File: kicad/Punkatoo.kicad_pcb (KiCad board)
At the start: 2 copper layers, 79 x 63.5 mm, 58 parts, among them J1 AC, J2 I/O, J3 FTDI, J4 IO 3.3v, J5 IO GND, J6 I2C, J7 Output, K1 G3MB, K2 G3MB, K3 G3MB, K4 G3MB, K5 G3MB-Relay_SolidState, Q1 BC847, Q10 BC807, Q11 BC807, Q2 BC847, Q3 BC847, Q4 BC847, Q5 BC847, Q6 BC847, Q7 BC807, Q8 BC807, Q9 BC807, SW1 Reset, SW2 Flash, U1 ESP32-WROOM-32, U2 IR RX, U3 AMS1117-3.3

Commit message: ??
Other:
- net class Default removed

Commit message: physical switching
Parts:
- removed the C2 at (83.9, 107.1)
- removed Capacitor: Ceiling_Fan_Capacitor, punkatoo:Ceiling_Fan_Capacitor
- removed D2: IR TX, LED_THT:LED_D5.0mm
- removed the J3 at (122.8, 94.2)
- removed the J4 at (147.5, 113.1)
- removed the JP1 at (133.9, 100.1)
- removed the Q1 at (133.9, 106.4)
- removed the R2 at (129.7, 106.2)
- removed R6, R7: 10, Resistor_SMD:R_0805_2012Metric_Pad1.15x1.40mm_HandSolder
- removed R8: 1K, Resistor_SMD:R_0805_2012Metric_Pad1.15x1.40mm_HandSolder
- added C1: 100n, Capacitor_SMD:C_0805_2012Metric_Pad1.18x1.45mm_HandSolder, B.Cu at (111.0, 64.8)
- added C9: Capacitor, +Capacitor:3Wire_3uF+7uF, F.Cu at (81.6, 137.2)
- J1: value AC -> Serial; footprint Connector_Molex:Molex_KK-254_AE-6410-02A_1x02_P2.54mm_Vertical -> Connector_PinSocket_2.54mm:PinSocket_1x03_P2.54mm_Vertical
- J2: footprint Connector_PinHeader_2.54mm:PinHeader_2x05_P2.54mm_Vertical -> +Conn:Conn_03x06
- J4: renamed from J7; footprint Connector_Molex:Molex_KK-254_AE-6410-05A_1x05_P2.54mm_Vertical -> Connector_Molex:Molex_KK-254_AE-6410-03A_1x03_P2.54mm_Vertical
- J5: value IO GND -> Output; footprint Resistor_SMD:R_0805_2012Metric_Pad1.15x1.40mm_HandSolder -> Connector_Molex:Molex_KK-254_AE-6410-05A_1x05_P2.54mm_Vertical; moved to F.Cu
- K1, K2, K3, K4, K5: footprint Relay_SolidState+:G3MB -> +Relay:G3MB
- R1: value LDR -> 1k; footprint OptoDevice:R_LDR_5.1x4.3mm_P3.4mm_Vertical -> Resistor_SMD:R_0805_2012Metric_Pad1.20x1.40mm_HandSolder
- moved J5 76.0 mm to (77.7, 127.5), turned to 90 degrees
- moved J1 50.6 mm to (131.3, 95.8), turned to -90 degrees
- moved R1 37.0 mm to (124.0, 75.8), turned to 0 degrees
- moved REF** 22.0 mm to (76.0, 133.4)
- moved F1 20.1 mm to (92.7, 125.0), turned to 90 degrees
- moved REF** 18.4 mm to (130.2, 133.4)
- moved R3 16.1 mm to (133.1, 101.9)
- moved R4 13.8 mm to (130.6, 101.9), turned to -90 degrees
- moved R2 13.5 mm to (135.7, 101.9), turned to -90 degrees
- moved D1 9.37 mm to (135.7, 112.8)
- moved RV1 8.64 mm to (105.1, 109.7), turned to -90 degrees
- moved J4 4.85 mm to (77.7, 113.3)
- moved J2 4.32 mm to (142.2, 101.6)
- moved Q5 0.77 mm to (102.1, 97.2)
- moved Q4 0.71 mm to (102.1, 92.1)
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- renumbered C1 to C2, J6 to J3, JP3 to JP1, Q2 to Q1, Q11 to Q10, Q3 to Q2, Q4 to Q3, Q5 to Q4, Q6 to Q5, Q7 to Q6, Q8 to Q7, Q9 to Q8, Q10 to Q9, R10 to R12, R11 to R13, R12 to R14, R13 to R15, R14 to R16, R3 to R2, R4 to R3, R5 to R4
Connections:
- D1 pad 2: Net-(D1-Pad2) -> +3V3
- D1 pad 4: +3V3 -> Net-(D1-Pad4)
- F1 pad 2: Net-(F1-Pad2) -> FUSED
- J1 pad 1: NEUT -> /TXD
- J1 pad 2: Net-(F1-Pad2) -> /RXD
- J2 pad 2: Net-(J2-Pad10) -> Net-(J2-Pad2)
- J2 pad 4: Net-(J2-Pad10) -> Net-(J2-Pad4)
- J2 pad 5: Net-(J2-Pad5) -> Net-(U1-Pad8)
- J2 pad 6: Net-(J2-Pad10) -> Net-(U1-Pad37)
- J2 pad 7: Net-(J2-Pad7) -> +3V3
- J2 pad 8: Net-(J2-Pad10) -> GND
- J4 pad 1: Net-(C2-Pad3) -> /Red
- J4 pad 2: Net-(C2-Pad2) -> /Green
- J4 pad 3: /M1 -> /Blue
- J5 pad 1: GND -> NEUT
- J5 pad 2: Net-(J2-Pad10) -> LINE
- JP1 pad 2: LINE -> FUSED
- K1 pad 1: Net-(C2-Pad3) -> /Green
- K2 pad 1: Net-(C2-Pad2) -> /Blue
- K3 pad 1: /M1 -> /Red
- K3 pad 2: LINE -> FUSED
- K4 pad 2: LINE -> FUSED
- K5 pad 2: LINE -> FUSED
- PS1 pad 1: LINE -> FUSED
- R1 pad 1: +3V3 -> Net-(C1-Pad2)
- R1 pad 2: Net-(R1-Pad2) -> +3V3
- R2 pad 1: Net-(R3-Pad1) -> Net-(R2-Pad1)
- R3 pad 1: Net-(R4-Pad1) (its old number) -> Net-(R3-Pad1)
- R3 pad 2: Net-(D1-Pad2) -> Net-(D1-Pad3)
- R4 pad 2: Net-(D1-Pad3) -> Net-(D1-Pad4)
- RV1 pad 2: LINE -> FUSED
- SW1 pad 2: Net-(SW1-Pad2) -> Net-(C1-Pad2)
- U1 pad 13: Net-(U1-Pad13) -> unconnected-(U1-Pad13)
- U1 pad 14: Net-(R4-Pad1) (its old number) -> unconnected-(U1-Pad14)
- U1 pad 17: Net-(U1-Pad17) -> unconnected-(U1-Pad17)
- U1 pad 18: Net-(U1-Pad18) -> unconnected-(U1-Pad18)
- U1 pad 19: Net-(U1-Pad19) -> unconnected-(U1-Pad19)
- U1 pad 20: Net-(U1-Pad20) -> unconnected-(U1-Pad20)
- U1 pad 21: Net-(U1-Pad21) -> unconnected-(U1-Pad21)
- U1 pad 22: Net-(U1-Pad22) -> unconnected-(U1-Pad22)
- U1 pad 26: Net-(R8-Pad1) -> Net-(R2-Pad1)
- U1 pad 27: Net-(J2-Pad9) -> Net-(J2-Pad4)
- U1 pad 28: Net-(J2-Pad7) -> Net-(J2-Pad3)
- U1 pad 29: Net-(U1-Pad29) -> unconnected-(U1-Pad29)
- U1 pad 3: Net-(SW1-Pad2) -> Net-(C1-Pad2)
- U1 pad 30: Net-(J2-Pad5) -> Net-(J2-Pad2)
- U1 pad 31: Net-(J2-Pad3) -> Net-(J2-Pad1)
- U1 pad 32: Net-(U1-Pad32) -> unconnected-(U1-Pad32)
- U1 pad 37: Net-(J2-Pad1) -> Net-(U1-Pad37)
- U1 pad 4: Net-(U1-Pad4) -> unconnected-(U1-Pad4)
- U1 pad 5: Net-(U1-Pad5) -> unconnected-(U1-Pad5)
- U1 pad 7: Net-(R1-Pad2) -> unconnected-(U1-Pad7)
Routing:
- net Net-(C2-Pad3): track 59.1 -> 0.00 mm
- net Net-(R1-Pad2): track 54.9 -> 0.00 mm, vias 2 -> 0
- net Net-(C2-Pad2): track 54.2 -> 0.00 mm
- net FUSED: track 0.00 -> 48.7 mm
- net LINE: track 63.0 -> 15.0 mm
- net Net-(U1-Pad37): track 0.00 -> 46.4 mm, vias 0 -> 1
- net /Green: track 0.00 -> 44.3 mm
- net Net-(U1-Pad8): track 0.00 -> 43.6 mm, vias 0 -> 3
- net /Red: track 0.00 -> 43.5 mm
- net /M1: track 40.8 -> 0.00 mm
- net Net-(D1-Pad2): track 35.5 -> 0.00 mm, vias 1 -> 0
- net Net-(J2-Pad4): track 0.00 -> 33.4 mm, vias 0 -> 1
- net Net-(J2-Pad9): track 32.6 -> 0.00 mm, vias 1 -> 0
- net Net-(J2-Pad2): track 0.00 -> 31.4 mm, vias 0 -> 1
- net Net-(J2-Pad7): track 31.3 -> 0.00 mm, vias 1 -> 0
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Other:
- board size 79 x 63.5 mm -> 79 x 79.9 mm
- board text added: "Punkatoo 2.0 220407 © 2022"
- board text removed: "1"
- board text removed: "16"
- board text removed: "17"
- board text removed: "18"
- board text removed: "19"
- board text removed: "2"
- board text removed: "23"
- board text removed: "3/M1"
- board text removed: "4/M2"
- board text removed: "5/Lm"
- board text removed: "B"
- board text removed: "L"
- board text removed: "N"
- board text removed: "Punkatoo 0.1 210107 © 2021"
- board text removed: "R"
- board text removed: "RX"
- board text removed: "TX"
- board text removed: "V+"

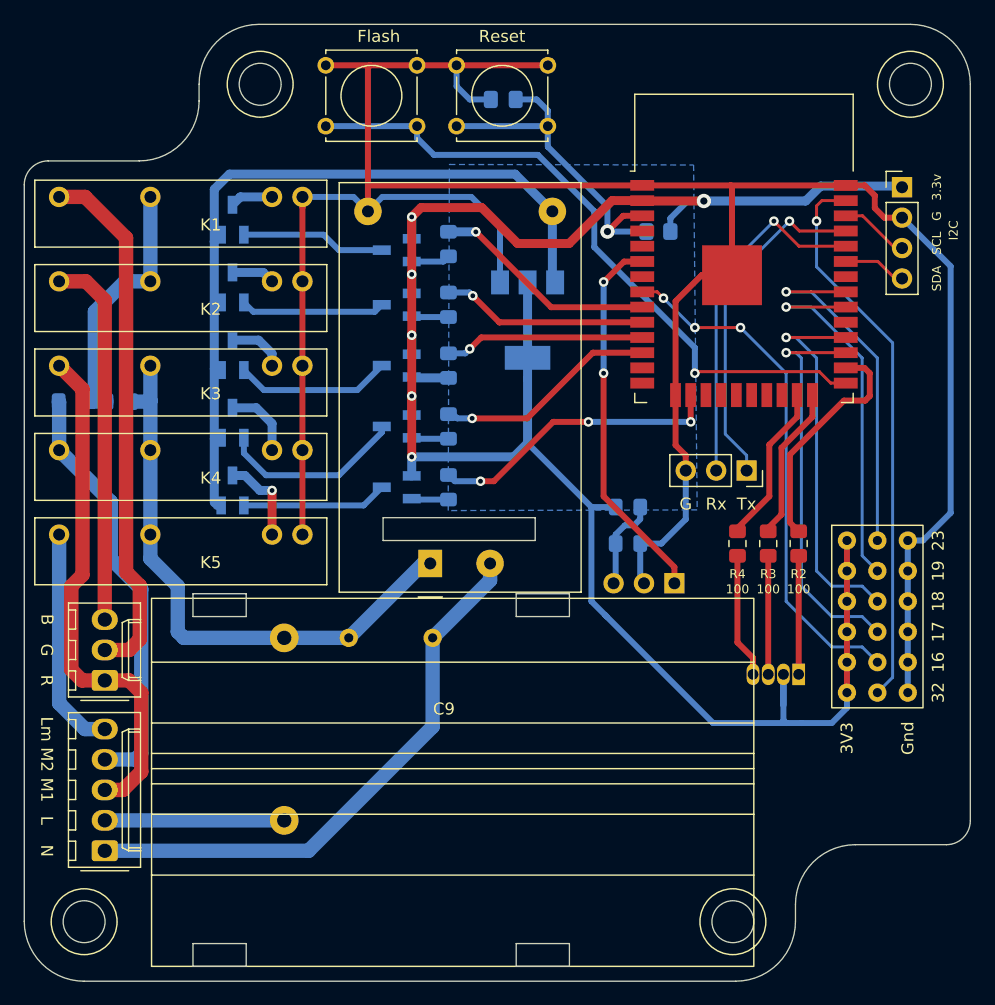
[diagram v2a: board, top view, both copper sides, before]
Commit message: Mods for update of ESP32 framework to 4.1.0
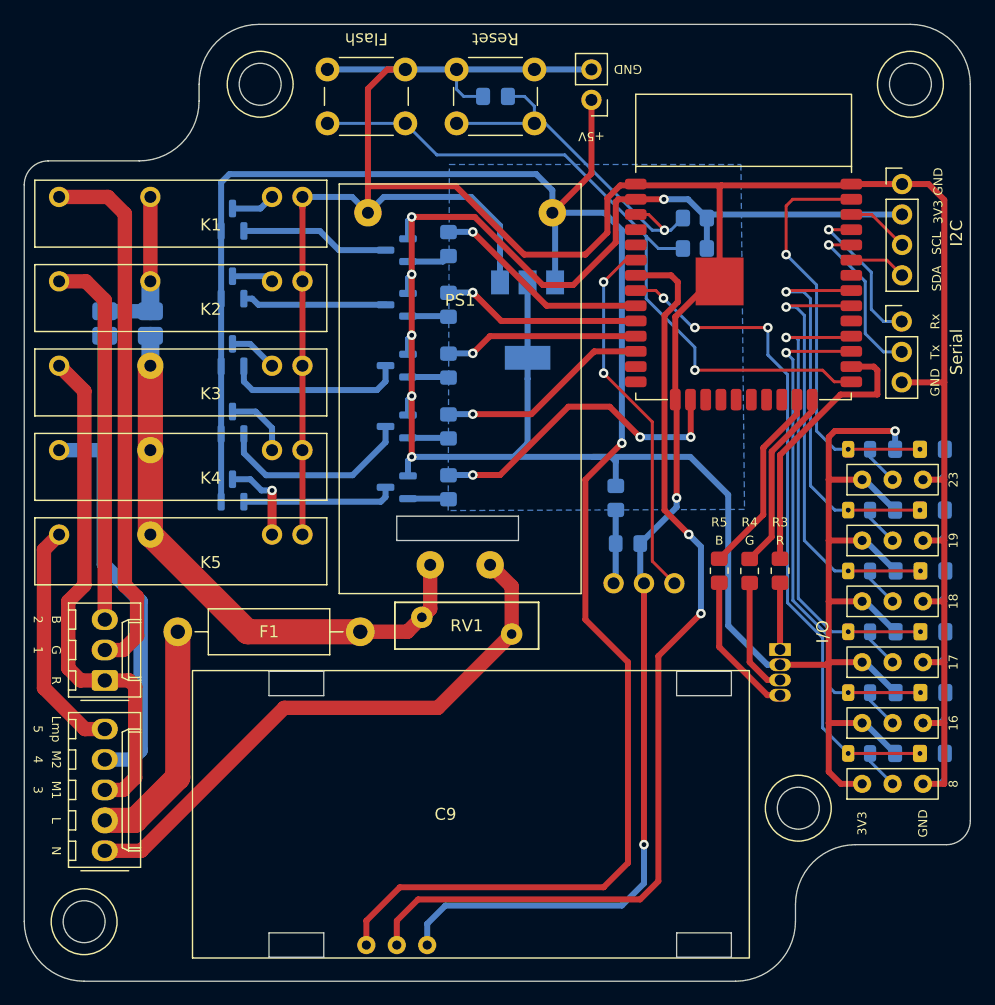
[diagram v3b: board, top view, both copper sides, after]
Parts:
- added C2: C_Option, +Capacitor:C_0805_Option, B.Cu at (145.8, 119.4)
- added C3: C_Option, +Capacitor:C_0805_Option, B.Cu at (145.8, 114.3)
- added C5: C_Option, +Capacitor:C_0805_Option, B.Cu at (145.8, 109.2)
- added C6: C_Option, +Capacitor:C_0805_Option, B.Cu at (145.8, 104.1)
- added C7: C_Option, +Capacitor:C_0805_Option, B.Cu at (145.8, 99.1)
- added C8: C_Option, +Capacitor:C_0805_Option, B.Cu at (145.8, 94.0)
- added J1: 5V Power, Connector_PinHeader_2.54mm:PinHeader_1x02_P2.54mm_Vertical, F.Cu at (118.4, 64.8)
- added R10: 1K, +Passive:R_0805+THT, B.Cu at (140.7, 104.1)
- added R11: 1K, +Passive:R_0805+THT, B.Cu at (140.7, 99.1)
- added R12: 1K, +Passive:R_0805+THT, B.Cu at (140.7, 94.0)
- added R2: 10k, Resistor_SMD:R_0805_2012Metric_Pad1.20x1.40mm_HandSolder, B.Cu at (127.0, 77.2)
- added R7: 1K, +Passive:R_0805+THT, B.Cu at (140.7, 119.4)
- added R8: 1K, +Passive:R_0805+THT, B.Cu at (140.7, 114.3)
- added R9: 1K, +Passive:R_0805+THT, B.Cu at (140.7, 109.2)
- added U2: PIR, +Sensor:PIR, B.Cu at (102.1, 136.7)
- C9: footprint +Capacitor:3Wire_3uF+7uF -> +Capacitor:3Wire_2.5uF+4.5uF
- F1: value Fuse -> 3A; moved to F.Cu
- J2: renamed from J1; footprint Connector_PinSocket_2.54mm:PinSocket_1x03_P2.54mm_Vertical -> Connector_PinHeader_2.54mm:PinHeader_1x03_P2.54mm_Vertical
- J5: renamed from J4; value Output -> Capacitor
- J6: renamed from J5; value Output -> A/C
- JP1: value Gen -> General
- PS1: footprint Converter_ACDC+:Converter_ACDC_HiLink_HLK-PMxx -> +PSU:HLK-PMxx
- Q1, Q10, Q2, Q3, Q4, Q5, Q6, Q7, Q8, Q9: footprint local:SOT-23_HandSoldering -> Package_TO_SOT_SMD:SOT-23
- R1: value 1k -> 10k
- R13: renamed from R12; footprint Resistor_SMD:R_0805_2012Metric_Pad1.15x1.40mm_HandSolder -> Resistor_SMD:R_0805_2012Metric_Pad1.20x1.40mm_HandSolder
- R14: renamed from R13; footprint Resistor_SMD:R_0805_2012Metric_Pad1.15x1.40mm_HandSolder -> Resistor_SMD:R_0805_2012Metric_Pad1.20x1.40mm_HandSolder
- R15: renamed from R14; footprint Resistor_SMD:R_0805_2012Metric_Pad1.15x1.40mm_HandSolder -> Resistor_SMD:R_0805_2012Metric_Pad1.20x1.40mm_HandSolder
- R16: renamed from R15; footprint Resistor_SMD:R_0805_2012Metric_Pad1.15x1.40mm_HandSolder -> Resistor_SMD:R_0805_2012Metric_Pad1.20x1.40mm_HandSolder
- R17: renamed from R16; footprint Resistor_SMD:R_0805_2012Metric_Pad1.15x1.40mm_HandSolder -> Resistor_SMD:R_0805_2012Metric_Pad1.20x1.40mm_HandSolder
- R3: renamed from R2; value 100 -> R; footprint Resistor_SMD:R_0805_2012Metric_Pad1.15x1.40mm_HandSolder -> Resistor_SMD:R_0805_2012Metric_Pad1.20x1.40mm_HandSolder
- R4: renamed from R3; value 100 -> G; footprint Resistor_SMD:R_0805_2012Metric_Pad1.15x1.40mm_HandSolder -> Resistor_SMD:R_0805_2012Metric_Pad1.20x1.40mm_HandSolder
- R5: renamed from R4; value 100 -> B; footprint Resistor_SMD:R_0805_2012Metric_Pad1.15x1.40mm_HandSolder -> Resistor_SMD:R_0805_2012Metric_Pad1.20x1.40mm_HandSolder
- R6: renamed from R9; footprint Resistor_SMD:R_0805_2012Metric_Pad1.15x1.40mm_HandSolder -> Resistor_SMD:R_0805_2012Metric_Pad1.20x1.40mm_HandSolder
- RV1: footprint punkatoo:varistor_10mm -> Varistor:RV_Disc_D12mm_W3.9mm_P7.5mm; moved to F.Cu
- SW1, SW2: footprint Button_Switch_THT:SW_Tactile_Straight_KSL0Axx1LFTR -> Button_Switch_THT:SW_PUSH_6mm_H5mm
- U1: footprint RF_Module:ESP32-WROOM-32 -> +MCU:wroom32
- moved J2 18.0 mm to (144.3, 83.3), turned to 0 degrees
- moved F1 17.0 mm to (99.1, 109.2), turned to 180 degrees
- moved C9 13.2 mm to (85.0, 124.5)
- moved REF** 10.9 mm to (135.6, 124.0)
- moved JP2 7.10 mm to (77.7, 83.5), turned to -90 degrees
- moved JP1 7.03 mm to (81.5, 83.5), turned to -90 degrees
- moved RV1 6.61 mm to (111.7, 109.4), turned to 180 degrees
- moved J3 5.24 mm to (143.5, 96.5)
- moved R1 3.25 mm to (127.0, 74.7)
- moved U1 2.98 mm to (131.1, 77.2)
- moved R4 2.76 mm to (131.6, 104.1)
- moved R3 2.75 mm to (134.1, 104.1)
- moved R5 2.73 mm to (129.0, 104.1)
- moved D1 2.59 mm to (134.1, 110.7), turned to -90 degrees
- moved R6 1.27 mm to (120.4, 98.0), turned to -90 degrees
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- renumbered C2 to C4, J2 to J3, J3 to J4, U2 to U3, U3 to U4
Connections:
- net /Blue renamed /C_Blue
- net /FLASH renamed /Flash
- net /Green renamed /C_Green
- net /Red renamed /C_Red
- net NEUT renamed Neutral
- net Net-(C1-Pad2) renamed /Reset
- net Net-(R2-Pad1) renamed /IndR
- net Net-(R3-Pad1) renamed /IndG
- net Net-(R4-Pad1) renamed /IndB
- net Net-(U1-Pad6) renamed /IR
- F1 pad 1: LINE -> Fused
- F1 pad 2: FUSED -> /LINE
- J3 pad 1: Net-(J2-Pad1) -> Net-(J3-Pad1)
- J3 pad 2: Net-(J2-Pad2) -> Net-(J3-Pad2)
- J3 pad 3: Net-(J2-Pad3) -> Net-(J3-Pad3)
- J3 pad 4: Net-(J2-Pad4) -> Net-(J3-Pad4)
- J3 pad 5: Net-(U1-Pad8) -> Net-(J3-Pad5)
- J3 pad 6: Net-(U1-Pad37) -> Net-(J3-Pad6)
- J4 pad 1: +3V3 -> GND
- J4 pad 2: GND -> +3V3
- J6 pad 2: LINE -> /LINE
- JP1 pad 2: FUSED -> Fused
- K3 pad 2: FUSED -> Fused
- K4 pad 2: FUSED -> Fused
- K5 pad 2: FUSED -> Fused
- PS1 pad 1: FUSED -> Fused
- RV1 pad 2: FUSED -> Fused
- U1 pad 27: Net-(J2-Pad4) -> /16
- U1 pad 28: Net-(J2-Pad3) -> /17
- U1 pad 30: Net-(J2-Pad2) -> /18
- U1 pad 31: Net-(J2-Pad1) -> /19
- U1 pad 37: Net-(U1-Pad37) -> /23
- U1 pad 7: unconnected-(U1-Pad7) -> /PIR
- U1 pad 8: Net-(U1-Pad8) -> /8
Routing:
- net GND: track 217.0 -> 316.8 mm, vias 0 -> 2
- net +5V: track 65.5 -> 161.4 mm, vias 0 -> 1
- net /PIR: track 0.00 -> 82.2 mm, vias 0 -> 2
- net /8: track 0.00 -> 56.6 mm, vias 0 -> 3
- net +3V3: track 164.5 -> 219.6 mm, vias 6 -> 7
- net FUSED: track 48.7 -> 0.00 mm
- net Fused: track 0.00 -> 47.8 mm
- net Net-(U1-Pad37): track 46.4 -> 0.00 mm, vias 1 -> 0
- net Net-(U1-Pad8): track 43.6 -> 0.00 mm, vias 3 -> 0
- net /16: track 0.00 -> 42.7 mm, vias 0 -> 1
- net /17: track 0.00 -> 39.0 mm, vias 0 -> 1
- net /18: track 0.00 -> 36.8 mm, vias 0 -> 1
- net /23: track 0.00 -> 34.8 mm, vias 0 -> 1
- net Net-(J2-Pad4): track 33.4 -> 0.00 mm, vias 1 -> 0
- net /19: track 0.00 -> 33.4 mm, vias 0 -> 1
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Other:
- outline, holes or cut-outs redrawn
- board text added: "3V3"
- board text added: "GND"
- board text added: "Input Filters"
- board text removed: "3.3v"
- board text removed: "G"

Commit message: V2.0 PCB prepared for manufacture
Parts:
- K1, K2, K3, K4: value G3MB -> G3MB-Relay_SolidState
- moved REF** 9.03 mm to (134.4, 132.9)
- moved U3 5.13 mm to (120.2, 105.2), turned to 0 degrees
- moved G*** 3.54 mm to (139.2, 66.8)
- moved REF** 3.25 mm to (89.5, 66.5)
- moved REF** 3.12 mm to (145.9, 66.5)
- moved J1 2.77 mm to (118.1, 67.6)
- moved C9 2.25 mm to (82.8, 124.5)
- moved REF** 1.13 mm to (75.0, 132.9)
- moved SW2 0.96 mm to (101.9, 66.8)
- moved C1 0.42 mm to (109.9, 64.5)
- moved SW1 0.42 mm to (106.7, 62.3)
- moved C4 0.26 mm to (121.7, 101.9)
- moved R6 0.25 mm to (120.6, 98.0)
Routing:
- net +5V: track 161.4 -> 152.2 mm, vias 1 -> 2
- net Net-(C4-Pad1): track 6.18 -> 12.0 mm
- net GND: track 316.8 -> 311.6 mm, vias 2 -> 1
- net /PIR: track 82.2 -> 77.5 mm, vias 2 -> 1
- net +3V3: track 219.6 -> 216.3 mm
- net /Flash: track 60.3 -> 62.3 mm
- net Net-(D1-Pad4): track 12.1 -> 12.7 mm
- net /IR: track 31.0 -> 31.6 mm
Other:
- board size 79 x 79.9 mm -> 78.9 x 78.4 mm
- board text added: "Punkatoo 2.0 260407 © 2022"
- board text removed: "Punkatoo 2.0 220407 © 2022"
